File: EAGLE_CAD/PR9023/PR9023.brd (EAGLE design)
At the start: 62.4 x 63.2 mm, 75 parts, among them SW1 ESWT_TL3315

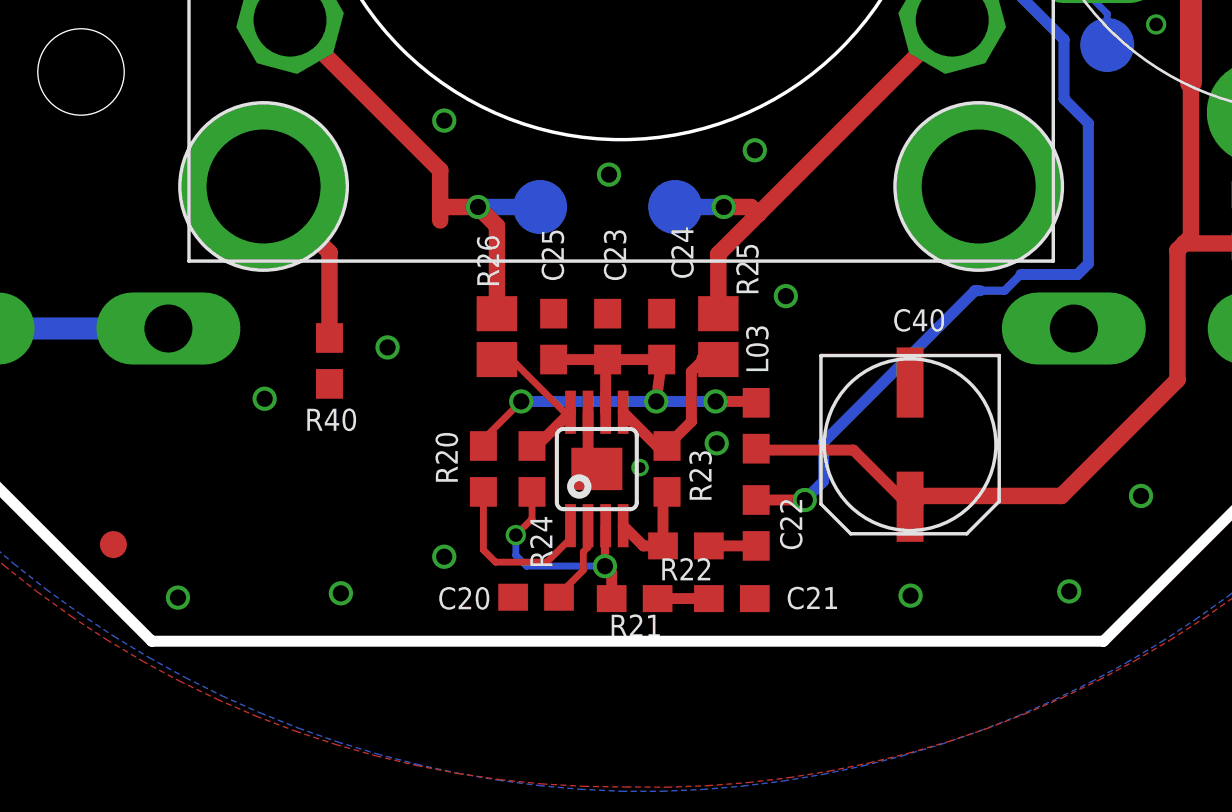
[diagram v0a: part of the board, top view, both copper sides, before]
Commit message: Updated Layout
Reworked amp layout (partially complete)
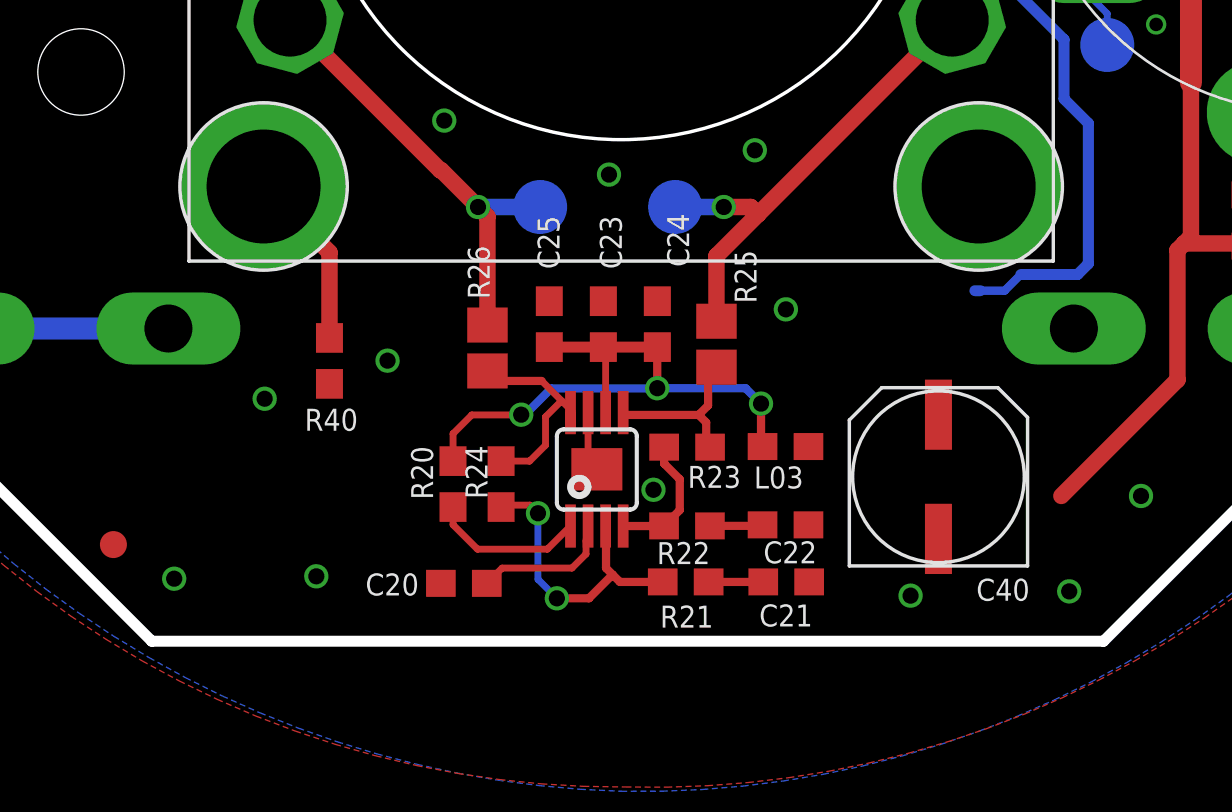
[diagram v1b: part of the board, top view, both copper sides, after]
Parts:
- moved C20 2.72 mm to (29.2, 7.06)
- moved C21 2.10 mm to (41.1, 7.12)
- moved R21 1.99 mm to (37.4, 7.12)
- moved C40 1.59 mm to (46.8, 11.0), turned to 0 degrees
- moved L03 1.33 mm to (41.1, 12.1), turned to 180 degrees
- moved R24 1.27 mm to (30.6, 10.7)
- moved R20 1.26 mm to (28.8, 10.7)
- moved R23 1.10 mm to (37.4, 12.1), turned to 0 degrees
- moved C22 1.09 mm to (41.1, 9.23), turned to 0 degrees
- moved R22 0.74 mm to (37.4, 9.19)
- moved R26 0.55 mm to (30.1, 15.8)
- moved U$1 0.49 mm to (33.5, 11.8)
- moved C23 0.49 mm to (34.3, 16.7)
- moved C24 0.49 mm to (36.3, 16.7)
- moved C25 0.49 mm to (32.3, 16.7)
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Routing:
- net VCC: track 110.5 -> 98.1 mm
- net A_OUT: track 40.9 -> 28.7 mm, vias 1 -> 0
- net N$2: track 18.5 -> 23.0 mm
- net N$11: track 5.50 -> 7.96 mm
- net N$5: track 8.88 -> 11.3 mm
- net N$12: track 3.20 -> 5.17 mm
- net N$14: track 3.85 -> 5.31 mm
- net N$20: track 6.76 -> 5.73 mm
- net SPK_OUT-: track 17.7 -> 16.6 mm
- net GND: track 15.8 -> 16.1 mm, vias 71 -> 69

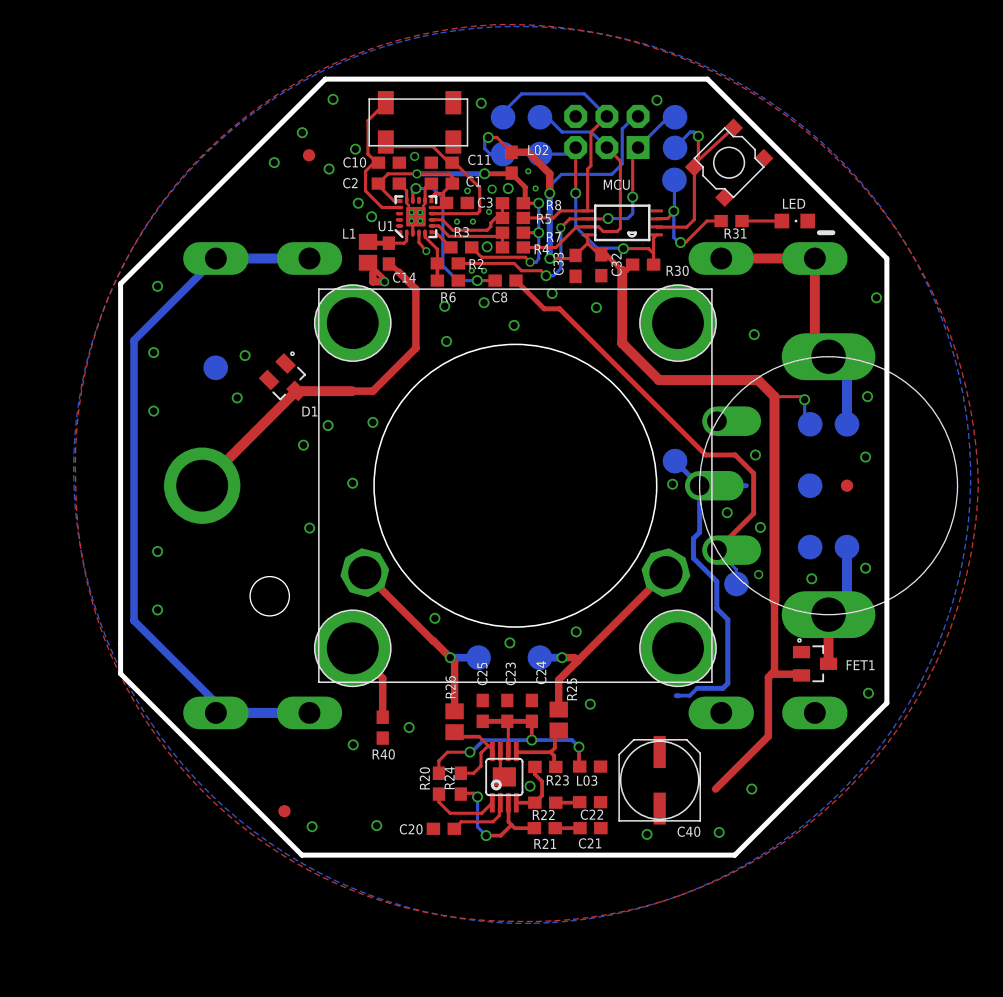
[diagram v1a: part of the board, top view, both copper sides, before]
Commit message: Small updates to the layout
Moved some of the traces around the amp and cleaned up the board
outline
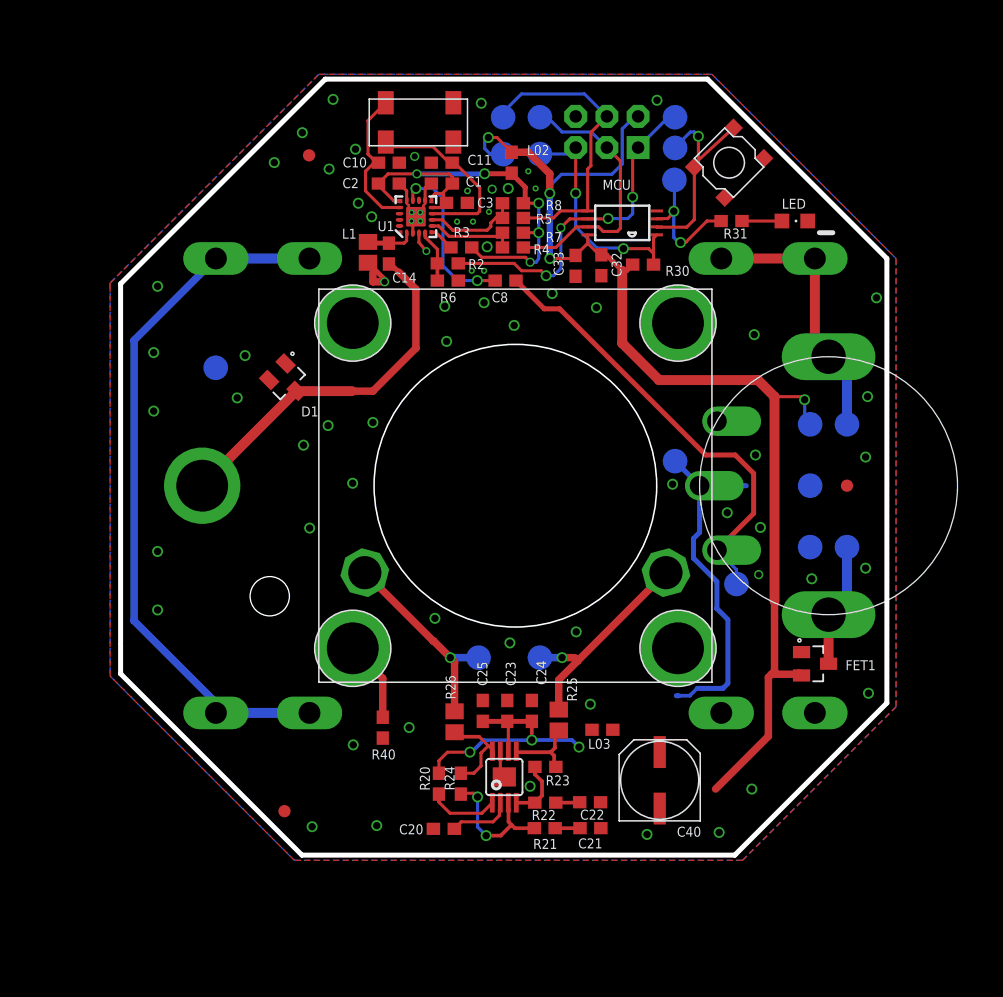
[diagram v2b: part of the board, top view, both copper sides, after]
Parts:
- moved L03 3.16 mm to (42.1, 15.1)
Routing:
- net N$2: track 23.0 -> 21.4 mm
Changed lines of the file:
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@@
 <setting verticaltext="up"/>
 </settings>
-<grid distance="0.07" unitdist="mm" unit="mm" style="lines" multiple="1" display="yes" altdistance="0.025" altunitdist="inch" altunit="inch"/>
+<grid distance="0.5" unitdist="mm" unit="mm" style="lines" multiple="1" display="yes" altdistance="0.025" altunitdist="inch" altunit="inch"/>
 <layers>
 <layer number="1" name="Top" color="4" fill="1" visible="yes" active="yes"/>
@@
 <attribute name="DCR" value="2.3" x="34.7" y="61.3" size="1.778" layer="27" rot="R270" display="off"/>
 </element>
-<element name="L03" library="PR_Parts_Library" package="0603_CPL" value="2.2k@100MHz" x="41.0875" y="12.13" smashed="yes" rot="R180">
-<attribute name="NAME" x="39.9165" y="10.578" size="0.8128" layer="25" font="vector" ratio="16"/>
-<attribute name="VALUE" x="42.1035" y="13.273" size="0.4064" layer="27" font="vector" rot="R180"/>
-<attribute name="MFG_PN" value="HZ0603A222R-10" x="41.0875" y="12.13" size="1.778" layer="27" rot="R180" display="off"/>
-<attribute name="CURRENT" value="150mA" x="41.0875" y="12.13" size="1.778" layer="27" rot="R180" display="off"/>
-<attribute name="TOL" value="" x="41.0875" y="12.13" size="1.778" layer="27" rot="R180" display="off"/>
-<attribute name="DCR" value="2.3" x="41.0875" y="12.13" size="1.778" layer="27" rot="R180" display="off"/>
+<element name="L03" library="PR_Parts_Library" package="0603_CPL" value="2.2k@100MHz" x="42.0875" y="15.13" smashed="yes" rot="R180">
+<attribute name="NAME" x="40.9165" y="13.578" size="0.8128" layer="25" font="vector" ratio="16"/>
+<attribute name="VALUE" x="43.1035" y="16.273" size="0.4064" layer="27" font="vector" rot="R180"/>
+<attribute name="MFG_PN" value="HZ0603A222R-10" x="42.0875" y="15.13" size="1.778" layer="27" rot="R180" display="off"/>
+<attribute name="CURRENT" value="150mA" x="42.0875" y="15.13" size="1.778" layer="27" rot="R180" display="off"/>
+<attribute name="TOL" value="" x="42.0875" y="15.13" size="1.778" layer="27" rot="R180" display="off"/>
+<attribute name="DCR" value="2.3" x="42.0875" y="15.13" size="1.778" layer="27" rot="R180" display="off"/>
 </element>
 <element name="R20" library="PR_Parts_Library" package="0603_CPL" value="10K" x="28.775" y="10.74" smashed="yes" rot="R90">
@@
 <via x="21.8" y="13.9" extent="1-16" drill="0.6"/>
 <via x="39.95" y="23.1" extent="1-16" drill="0.6"/>
-<polygon width="0.4064" layer="16">
-<vertex x="-0.9525" y="37.38125" curve="90"/>
-<vertex x="35" y="-0.635" curve="90"/>
-<vertex x="72.06375" y="35" curve="90"/>
-<vertex x="36.11125" y="72.38125" curve="90"/>
-</polygon>
-<polygon width="0.4064" layer="1">
-<vertex x="-0.79375" y="35" curve="90"/>
-<vertex x="35.15875" y="-0.47625" curve="90"/>
-<vertex x="72.69875" y="35.15875" curve="90"/>
-<vertex x="33.4125" y="72.54" curve="90"/>
-</polygon>
 <via x="52.25" y="32.8" extent="1-16" drill="0.6"/>
 <via x="20.15375" y="66.45375" extent="1-16" drill="0.6"/>
@@
 <wire x1="33.775" y1="11.61125" x2="34.1" y2="11.28625" width="0.254" layer="1"/>
 <via x="36.1975" y="10.52875" extent="1-16" drill="0.6"/>
+<polygon width="0.6096" layer="16">
+<vertex x="2" y="51.5"/>
+<vertex x="2" y="19.5"/>
+<vertex x="17" y="4.5"/>
+<vertex x="53.5" y="4.5"/>
+<vertex x="66" y="17"/>
+<vertex x="66" y="53.5"/>
+<vertex x="51" y="68.5"/>
+<vertex x="19" y="68.5"/>
+</polygon>
+<polygon width="0.6096" layer="1">
+<vertex x="2" y="51"/>
+<vertex x="2" y="51.5"/>
+<vertex x="19" y="68.5"/>
+<vertex x="51" y="68.5"/>
+<vertex x="66" y="53.5"/>
+<vertex x="66" y="17"/>
+<vertex x="53.5" y="4.5"/>
+<vertex x="17" y="4.5"/>
+<vertex x="2" y="19.5"/>
+</polygon>
+<wire x1="58.3" y1="21.45" x2="59.384" y2="16.5" width="0" layer="19" extent="1-1"/>
 </signal>
 <signal name="N$1">
@@
 <wire x1="44.05" y1="52.5" x2="44.55" y2="53" width="0.4064" layer="1"/>
 <wire x1="46.75" y1="13.31" x2="51.3" y2="10.3" width="0" layer="19" extent="1-1"/>
-<wire x1="41.9375" y1="12.13" x2="46.75" y2="13.31" width="0" layer="19" extent="1-1"/>
+<wire x1="42.9375" y1="15.13" x2="46.75" y2="13.31" width="0" layer="19" extent="1-1"/>
 </signal>
 <signal name="N$20">
@@
 <wire x1="39.61" y1="14.29" x2="40.18" y2="13.72" width="0.3048" layer="16"/>
 <via x="40.18" y="13.72" extent="1-16" drill="0.6"/>
-<wire x1="40.18" y1="13.72" x2="40.18" y2="12.1875" width="0.3048" layer="1"/>
-<wire x1="40.18" y1="12.1875" x2="40.2375" y2="12.13" width="0.3048" layer="1"/>
+<wire x1="40.18" y1="13.72" x2="41.2375" y2="15.13" width="0" layer="19" extent="1-1"/>
 </signal>
 <signal name="N$12">

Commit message: first update in a while from my end
the big change here is the speaker footprint itself. i updated that to
fit Fun’s redesign. i also made some smallish changes to the board
perimeter and a few of the things inside it - mostly very small changes.
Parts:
- removed U$2, U$3, U$4: PEM_M3_NOPIN, PR_Parts_Library:PEM_M3_NOKEEPAWAY
- moved U$5 60.4 mm to (81.8, 28.8)
- moved L03 3.16 mm to (41.1, 12.1)
- moved U$1 1.70 mm to (35.0, 11.0), turned to 0 degrees
- moved C40 1.50 mm to (46.8, 9.51)
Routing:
- net VCC: track 98.1 -> 107.0 mm
- net A_OUT: track 28.7 -> 37.4 mm, vias 0 -> 1
- net N$6: track 6.62 -> 3.17 mm
- net N$2: track 21.4 -> 23.0 mm
- net GND: track 16.1 -> 14.6 mm
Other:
- board size 62.4 x 63.2 mm -> 70 x 70 mm
- board text added: "PR9023 Born + tuned in Brooklyn http://thepublicrad.io"
- board text removed: "PR9020 Born + tuned in Brooklyn http://thepublicrad.io"
